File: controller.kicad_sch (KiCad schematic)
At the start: 18 parts, among them SW1 RotaryEncoder_Switch, U6 ATmega328P-P, U7 DS3231MZ

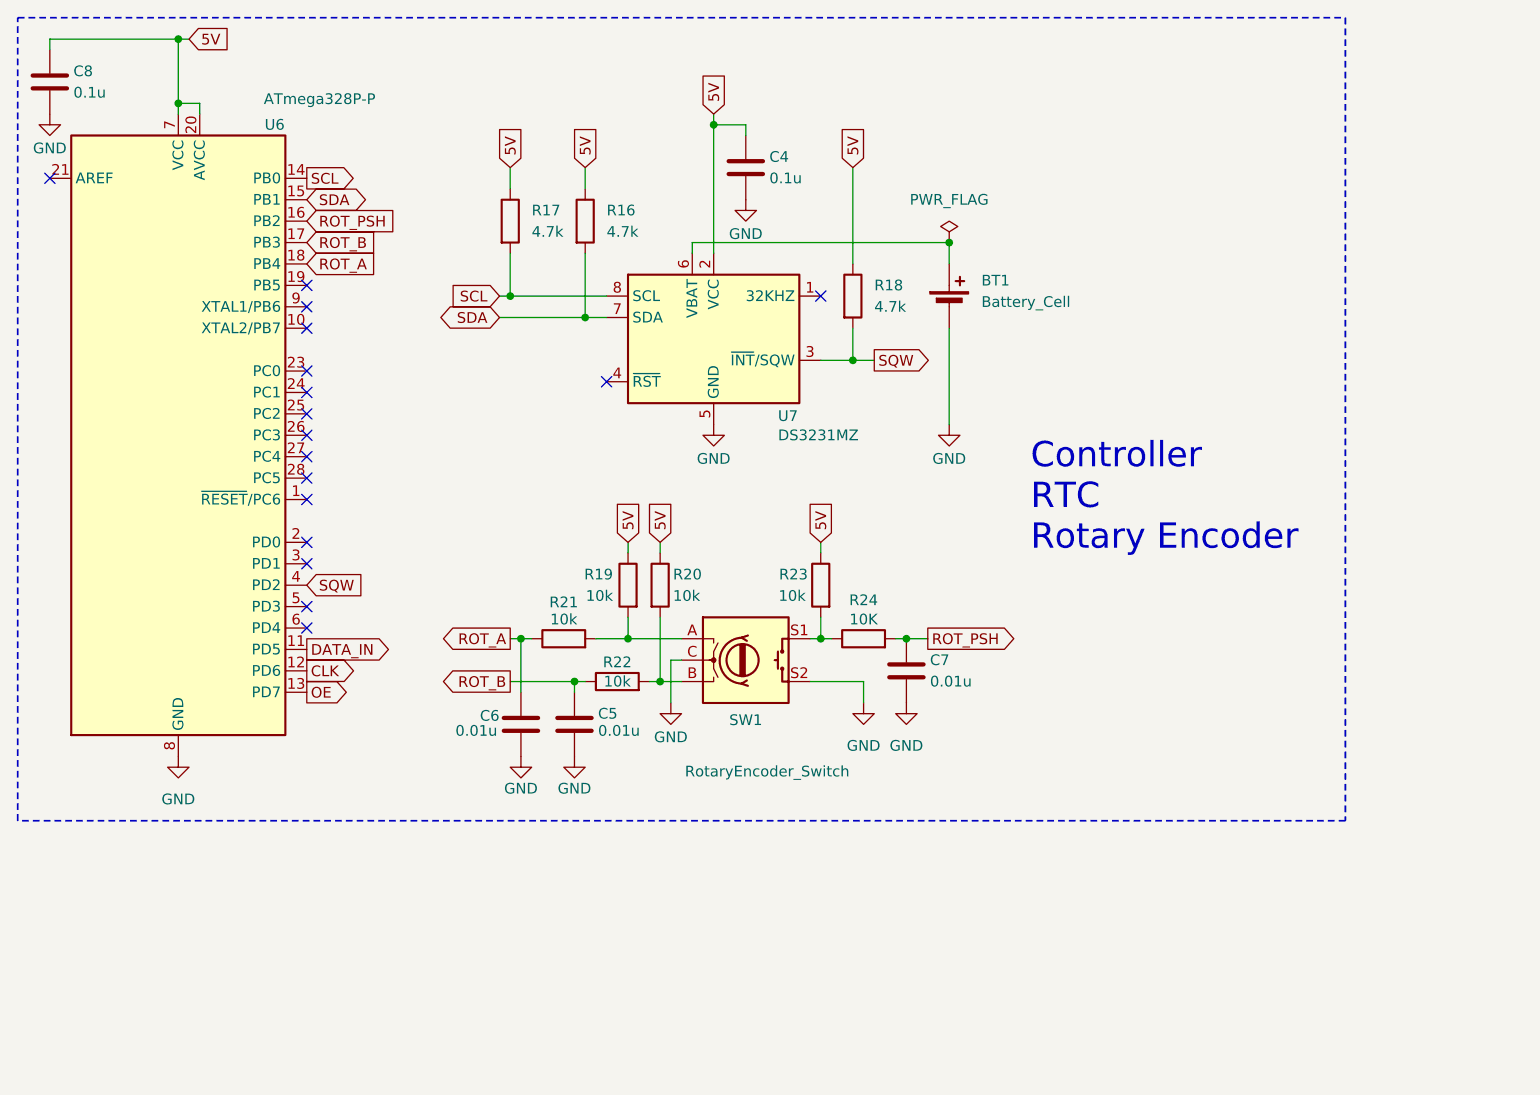
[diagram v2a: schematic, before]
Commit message: added footprints
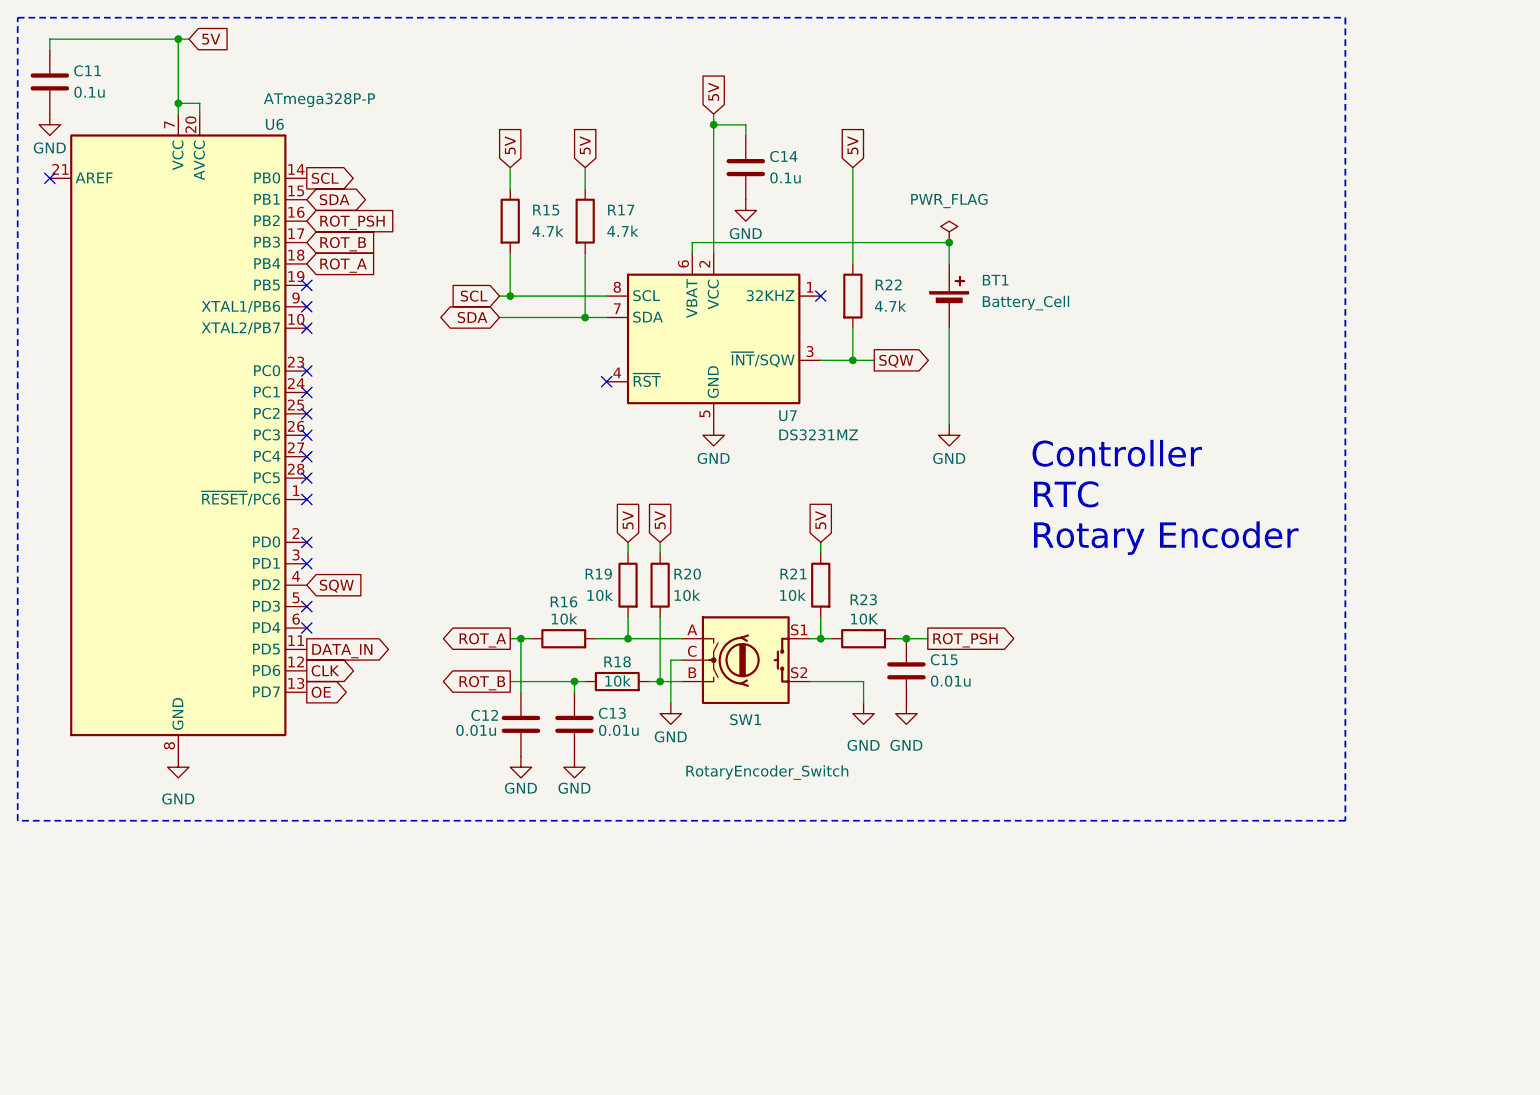
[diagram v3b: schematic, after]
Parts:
- BT1: footprint (none) -> nixie:BH-80B-1
- C11: renamed from C8; footprint (none) -> Capacitor_THT:C_Disc_D4.7mm_W2.5mm_P5.00mm
- C12: renamed from C6; footprint (none) -> Capacitor_THT:C_Disc_D4.7mm_W2.5mm_P5.00mm
- C13: renamed from C5; footprint (none) -> Capacitor_THT:C_Disc_D4.7mm_W2.5mm_P5.00mm
- C14: renamed from C4; footprint (none) -> Capacitor_THT:C_Disc_D4.7mm_W2.5mm_P5.00mm
- C15: renamed from C7; footprint (none) -> Capacitor_THT:C_Disc_D4.7mm_W2.5mm_P5.00mm
- R15: renamed from R17; footprint (none) -> Resistor_THT:R_Axial_DIN0207_L6.3mm_D2.5mm_P7.62mm_Horizontal
- R16: renamed from R21; footprint (none) -> Resistor_THT:R_Axial_DIN0207_L6.3mm_D2.5mm_P7.62mm_Horizontal
- R17: renamed from R16; footprint (none) -> Resistor_THT:R_Axial_DIN0207_L6.3mm_D2.5mm_P7.62mm_Horizontal
- R18: renamed from R22; footprint (none) -> Resistor_THT:R_Axial_DIN0207_L6.3mm_D2.5mm_P7.62mm_Horizontal
- R19, R20: footprint (none) -> Resistor_THT:R_Axial_DIN0207_L6.3mm_D2.5mm_P7.62mm_Horizontal
- R21: renamed from R23; footprint (none) -> Resistor_THT:R_Axial_DIN0207_L6.3mm_D2.5mm_P7.62mm_Horizontal
- R22: renamed from R18; footprint (none) -> Resistor_THT:R_Axial_DIN0207_L6.3mm_D2.5mm_P7.62mm_Horizontal
- R23: renamed from R24; footprint (none) -> Resistor_THT:R_Axial_DIN0207_L6.3mm_D2.5mm_P7.62mm_Horizontal
- SW1: footprint (none) -> nixie:PEC11H4020FS0016
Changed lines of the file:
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@@
 		(dnp no)
 		(fields_autoplaced yes)
-		(property "Reference" "R18"
+		(property "Reference" "R22"
 			(at 115.57 46.9899 0)
 			(effects
@@
 			)
 		)
-		(property "Footprint" ""
+		(property "Footprint" "Resistor_THT:R_Axial_DIN0207_L6.3mm_D2.5mm_P7.62mm_Horizontal"
 			(at 111.252 48.26 90)
 			(effects
@@
 			(project "nixie"
 				(path "/4d215aa3-d175-40c4-bbb4-87e7c6a030b1/e9b2c7e8-8fee-4f00-9fb9-8c32147df66b"
-					(reference "R18")
+					(reference "R22")
 					(unit 1)
 				)
@@
 		(on_board yes)
 		(dnp no)
-		(property "Reference" "#PWR018"
+		(property "Reference" "#PWR022"
 			(at 91.44 102.87 0)
 			(effects
@@
 			(project ""
 				(path "/4d215aa3-d175-40c4-bbb4-87e7c6a030b1/e9b2c7e8-8fee-4f00-9fb9-8c32147df66b"
-					(reference "#PWR018")
+					(reference "#PWR022")
 					(unit 1)
 				)
@@
 		(on_board yes)
 		(dnp no)
-		(property "Reference" "C4"
+		(property "Reference" "C14"
 			(at 103.124 31.75 0)
 			(effects
@@
 			)
 		)
-		(property "Footprint" ""
+		(property "Footprint" "Capacitor_THT:C_Disc_D4.7mm_W2.5mm_P5.00mm"
 			(at 101.2952 36.83 0)
 			(effects
@@
 			(project ""
 				(path "/4d215aa3-d175-40c4-bbb4-87e7c6a030b1/e9b2c7e8-8fee-4f00-9fb9-8c32147df66b"
-					(reference "C4")
+					(reference "C14")
 					(unit 1)
 				)
@@
 		(on_board yes)
 		(dnp no)
-		(property "Reference" "C7"
+		(property "Reference" "C15"
 			(at 122.174 91.44 0)
 			(effects
@@
 			)
 		)
-		(property "Footprint" ""
+		(property "Footprint" "Capacitor_THT:C_Disc_D4.7mm_W2.5mm_P5.00mm"
 			(at 120.3452 96.52 0)
 			(effects
@@
 			(project "nixie"
 				(path "/4d215aa3-d175-40c4-bbb4-87e7c6a030b1/e9b2c7e8-8fee-4f00-9fb9-8c32147df66b"
-					(reference "C7")
+					(reference "C15")
 					(unit 1)
 				)
@@
 			)
 		)
-		(property "Footprint" ""
+		(property "Footprint" "Resistor_THT:R_Axial_DIN0207_L6.3mm_D2.5mm_P7.62mm_Horizontal"
 			(at 88.138 82.55 90)
 			(effects
@@
 		(dnp no)
 		(fields_autoplaced yes)
-		(property "Reference" "#PWR019"
+		(property "Reference" "#PWR025"
 			(at 114.3 102.87 0)
 			(effects
@@
 			(project "nixie"
 				(path "/4d215aa3-d175-40c4-bbb4-87e7c6a030b1/e9b2c7e8-8fee-4f00-9fb9-8c32147df66b"
-					(reference "#PWR019")
+					(reference "#PWR025")
 					(unit 1)
 				)
@@
 		(on_board yes)
 		(dnp no)
-		(property "Reference" "#PWR024"
+		(property "Reference" "#PWR018"
 			(at 17.78 33.02 0)
 			(effects
@@
 			(project "nixie"
 				(path "/4d215aa3-d175-40c4-bbb4-87e7c6a030b1/e9b2c7e8-8fee-4f00-9fb9-8c32147df66b"
-					(reference "#PWR024")
+					(reference "#PWR018")
 					(unit 1)
 				)
@@
 		(on_board yes)
 		(dnp no)
-		(property "Reference" "C8"
+		(property "Reference" "C11"
 			(at 20.574 21.59 0)
 			(effects
@@
 			)
 		)
-		(property "Footprint" ""
+		(property "Footprint" "Capacitor_THT:C_Disc_D4.7mm_W2.5mm_P5.00mm"
 			(at 18.7452 26.67 0)
 			(effects
@@
 			(project "nixie"
 				(path "/4d215aa3-d175-40c4-bbb4-87e7c6a030b1/e9b2c7e8-8fee-4f00-9fb9-8c32147df66b"
-					(reference "C8")
+					(reference "C11")
 					(unit 1)
 				)
@@
 		(dnp no)
 		(fields_autoplaced yes)
-		(property "Reference" "R16"
+		(property "Reference" "R17"
 			(at 83.82 38.0999 0)
 			(effects
@@
 			)
 		)
-		(property "Footprint" ""
+		(property "Footprint" "Resistor_THT:R_Axial_DIN0207_L6.3mm_D2.5mm_P7.62mm_Horizontal"
 			(at 79.502 39.37 90)
 			(effects
@@
 			(project ""
 				(path "/4d215aa3-d175-40c4-bbb4-87e7c6a030b1/e9b2c7e8-8fee-4f00-9fb9-8c32147df66b"
-					(reference "R16")
+					(reference "R17")
 					(unit 1)
 				)
@@
 		(on_board yes)
 		(dnp no)
-		(property "Reference" "R21"
+		(property "Reference" "R16"
 			(at 78.74 84.582 90)
 			(effects
@@
 			)
 		)
-		(property "Footprint" ""
+		(property "Footprint" "Resistor_THT:R_Axial_DIN0207_L6.3mm_D2.5mm_P7.62mm_Horizontal"
 			(at 78.74 90.678 90)
 			(effects
@@
 			(project ""
 				(path "/4d215aa3-d175-40c4-bbb4-87e7c6a030b1/e9b2c7e8-8fee-4f00-9fb9-8c32147df66b"
-					(reference "R21")
+					(reference "R16")
 					(unit 1)
 				)
@@
 		(on_board yes)
 		(dnp no)
-		(property "Reference" "C6"
+		(property "Reference" "C12"
 			(at 71.12 98.044 0)
 			(effects
@@
 			)
 		)
-		(property "Footprint" ""
+		(property "Footprint" "Capacitor_THT:C_Disc_D4.7mm_W2.5mm_P5.00mm"
 			(at 72.6948 102.87 0)
 			(effects
@@
 			(project "nixie"
 				(path "/4d215aa3-d175-40c4-bbb4-87e7c6a030b1/e9b2c7e8-8fee-4f00-9fb9-8c32147df66b"
-					(reference "C6")
+					(reference "C12")
 					(unit 1)
 				)
@@
 		(on_board yes)
 		(dnp no)
-		(property "Reference" "#PWR020"
+		(property "Reference" "#PWR024"
 			(at 100.33 43.18 0)
 			(effects
@@
 			(project ""
 				(path "/4d215aa3-d175-40c4-bbb4-87e7c6a030b1/e9b2c7e8-8fee-4f00-9fb9-8c32147df66b"
-					(reference "#PWR020")
+					(reference "#PWR024")
 					(unit 1)
 				)
@@
 		(on_board yes)
 		(dnp no)
-		(property "Reference" "#PWR016"
+		(property "Reference" "#PWR023"
 			(at 96.52 69.85 0)
 			(effects
@@
 			(project "nixie"
 				(path "/4d215aa3-d175-40c4-bbb4-87e7c6a030b1/e9b2c7e8-8fee-4f00-9fb9-8c32147df66b"
-					(reference "#PWR016")
+					(reference "#PWR023")
 					(unit 1)
 				)
@@
 		(dnp no)
 		(fields_autoplaced yes)
-		(property "Reference" "#PWR023"
+		(property "Reference" "#PWR026"
 			(at 119.38 102.87 0)
 			(effects
@@
 			(project "nixie"
 				(path "/4d215aa3-d175-40c4-bbb4-87e7c6a030b1/e9b2c7e8-8fee-4f00-9fb9-8c32147df66b"
-					(reference "#PWR023")
+					(reference "#PWR026")
 					(unit 1)
 				)
@@
 		(on_board yes)
 		(dnp no)
-		(property "Reference" "C5"
+		(property "Reference" "C13"
 			(at 82.804 97.79 0)
 			(effects
@@
 			)
 		)
-		(property "Footprint" ""
+		(property "Footprint" "Capacitor_THT:C_Disc_D4.7mm_W2.5mm_P5.00mm"
 			(at 80.9752 102.87 0)
 			(effects
@@
 			(project ""
 				(path "/4d215aa3-d175-40c4-bbb4-87e7c6a030b1/e9b2c7e8-8fee-4f00-9fb9-8c32147df66b"
-					(reference "C5")
+					(reference "C13")
 					(unit 1)
 				)
@@
 		(dnp no)
 		(fields_autoplaced yes)
-		(property "Reference" "#PWR01"
+		(property "Reference" "#PWR019"
 			(at 33.02 109.22 0)
 			(effects
@@
 			(project ""
 				(path "/4d215aa3-d175-40c4-bbb4-87e7c6a030b1/e9b2c7e8-8fee-4f00-9fb9-8c32147df66b"
-					(reference "#PWR01")
+					(reference "#PWR019")
 					(unit 1)
 				)
@@
 			)
 		)
-		(property "Footprint" ""
+		(property "Footprint" "nixie:PEC11H4020FS0016"
 			(at 96.52 87.376 0)
 			(effects
@@
 		(on_board yes)
 		(dnp no)
-		(property "Reference" "R24"
+		(property "Reference" "R23"
 			(at 114.3 84.328 90)
 			(effects
@@
 			)
 		)
-		(property "Footprint" ""
+		(property "Footprint" "Resistor_THT:R_Axial_DIN0207_L6.3mm_D2.5mm_P7.62mm_Horizontal"
 			(at 114.3 90.678 90)
 			(effects
@@
 			(project ""
 				(path "/4d215aa3-d175-40c4-bbb4-87e7c6a030b1/e9b2c7e8-8fee-4f00-9fb9-8c32147df66b"
-					(reference "R24")
+					(reference "R23")
 					(unit 1)
 				)
@@
 		(on_board yes)
 		(dnp no)
-		(property "Reference" "R23"
+		(property "Reference" "R21"
 			(at 107.696 81.28 0)
 			(effects
@@
 			)
 		)
-		(property "Footprint" ""
+		(property "Footprint" "Resistor_THT:R_Axial_DIN0207_L6.3mm_D2.5mm_P7.62mm_Horizontal"
 			(at 110.998 82.55 90)
 			(effects
@@
 			(project "nixie"
 				(path "/4d215aa3-d175-40c4-bbb4-87e7c6a030b1/e9b2c7e8-8fee-4f00-9fb9-8c32147df66b"
-					(reference "R23")
+					(reference "R21")
 					(unit 1)
 				)
@@
 		(dnp no)
 		(fields_autoplaced yes)
-		(property "Reference" "R17"
+		(property "Reference" "R15"
 			(at 74.93 38.0999 0)
 			(effects
@@
 			)
 		)
-		(property "Footprint" ""
+		(property "Footprint" "Resistor_THT:R_Axial_DIN0207_L6.3mm_D2.5mm_P7.62mm_Horizontal"
 			(at 70.612 39.37 90)
 			(effects
@@
 			(project "nixie"
 				(path "/4d215aa3-d175-40c4-bbb4-87e7c6a030b1/e9b2c7e8-8fee-4f00-9fb9-8c32147df66b"
-					(reference "R17")
+					(reference "R15")
 					(unit 1)
 				)
@@
 			)
 		)
-		(property "Footprint" ""
+		(property "Footprint" "Resistor_THT:R_Axial_DIN0207_L6.3mm_D2.5mm_P7.62mm_Horizontal"
 			(at 88.392 82.55 90)
 			(effects
@@
 		(on_board yes)
 		(dnp no)
-		(property "Reference" "#PWR021"
+		(property "Reference" "#PWR020"
 			(at 73.66 109.22 0)
 			(effects
@@
 			(project "nixie"
 				(path "/4d215aa3-d175-40c4-bbb4-87e7c6a030b1/e9b2c7e8-8fee-4f00-9fb9-8c32147df66b"
-					(reference "#PWR021")
+					(reference "#PWR020")
 					(unit 1)
 				)
@@
 		(on_board yes)
 		(dnp no)
-		(property "Reference" "#PWR017"
+		(property "Reference" "#PWR027"
 			(at 124.46 69.85 0)
 			(effects
@@
 			(project "nixie"
 				(path "/4d215aa3-d175-40c4-bbb4-87e7c6a030b1/e9b2c7e8-8fee-4f00-9fb9-8c32147df66b"
-					(reference "#PWR017")
+					(reference "#PWR027")
 					(unit 1)
 				)
@@
 			)
 		)
-		(property "Footprint" ""
+		(property "Footprint" "nixie:BH-80B-1"
 			(at 124.46 48.006 90)
 			(effects
@@
 		(on_board yes)
 		(dnp no)
-		(property "Reference" "#PWR022"
+		(property "Reference" "#PWR021"
 			(at 80.01 109.22 0)
 			(effects
@@
 			(project "nixie"
 				(path "/4d215aa3-d175-40c4-bbb4-87e7c6a030b1/e9b2c7e8-8fee-4f00-9fb9-8c32147df66b"
-					(reference "#PWR022")
+					(reference "#PWR021")
 					(unit 1)
 				)
@@
 		(on_board yes)
 		(dnp no)
-		(property "Reference" "R22"
+		(property "Reference" "R18"
 			(at 85.09 91.694 90)
 			(effects
@@
 			)
 		)
-		(property "Footprint" ""
+		(property "Footprint" "Resistor_THT:R_Axial_DIN0207_L6.3mm_D2.5mm_P7.62mm_Horizontal"
 			(at 85.09 95.758 90)
 			(effects
@@
 			(project "nixie"
 				(path "/4d215aa3-d175-40c4-bbb4-87e7c6a030b1/e9b2c7e8-8fee-4f00-9fb9-8c32147df66b"
-					(reference "R22")
-					(unit 1)
-				)
+					(reference "R18")
+					(unit 1)
+				)

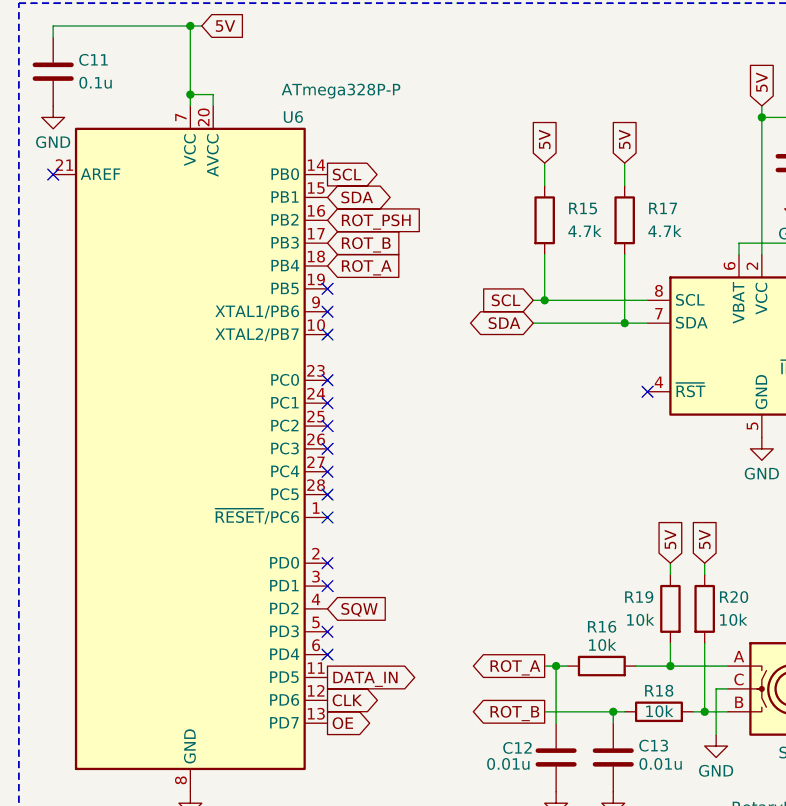
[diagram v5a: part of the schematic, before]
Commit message: connect scl sda to correct pins
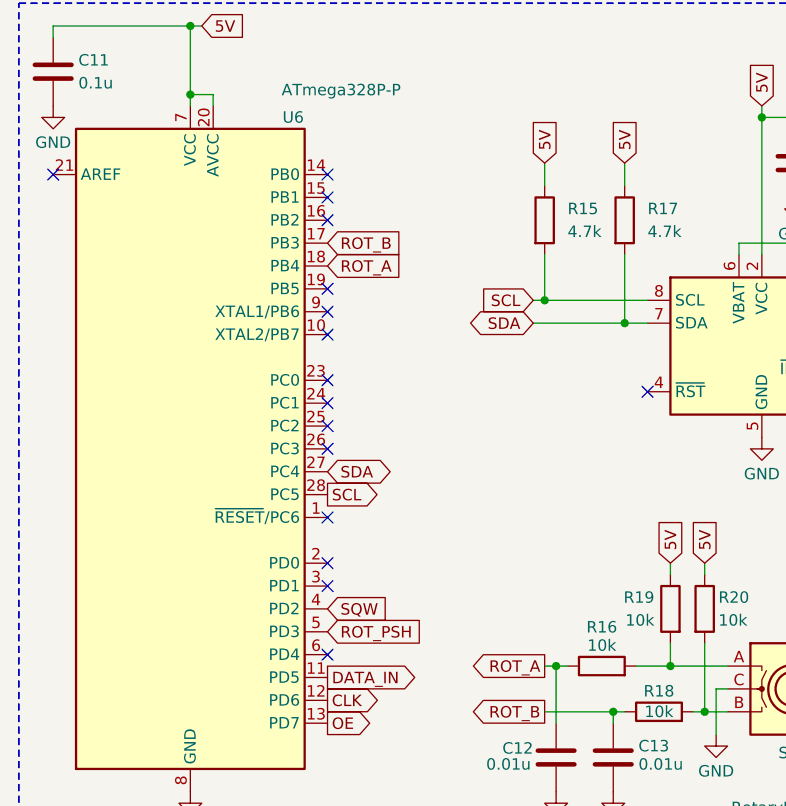
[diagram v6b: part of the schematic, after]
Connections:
- net ROT_PSH: now also U6.5 (PD3); no longer U6.16 (PB2)
- net SCL: now also U6.28 (PC5); no longer U6.14 (PB0)
- net SDA: now also U6.27 (PC4); no longer U6.15 (PB1)
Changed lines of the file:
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@@
+	)
+	(no_connect
+		(at 48.26 34.29)
 	)
 	(no_connect
@@
 	)
 	(no_connect
-		(at 48.26 85.09)
-	)
-	(no_connect
 		(at 48.26 77.47)
 	)
@@
 	)
 	(no_connect
+		(at 48.26 36.83)
+	)
+	(no_connect
 		(at 48.26 52.07)
 	)
 	(no_connect
-		(at 48.26 67.31)
-	)
-	(no_connect
 		(at 48.26 59.69)
 	)
@@
 	)
 	(no_connect
+		(at 48.26 39.37)
+	)
+	(no_connect
 		(at 17.78 34.29)
-	)
-	(no_connect
-		(at 48.26 69.85)
 	)
 	(wire
@@
 	(global_label "SDA"
 		(shape bidirectional)
-		(at 48.26 36.83 0)
-		(fields_autoplaced yes)
-		(effects
-			(font
-				(size 1.27 1.27)
-			)
-			(justify left)
-		)
-		(property "Intersheetrefs" "${INTERSHEET_REFS}"
-			(at 55.9246 36.83 0)
+		(at 48.26 67.31 0)
+		(fields_autoplaced yes)
+		(effects
+			(font
+				(size 1.27 1.27)
+			)
+			(justify left)
+		)
+		(property "Intersheetrefs" "${INTERSHEET_REFS}"
+			(at 55.9246 67.31 0)
 			(effects
 				(font
@@
 	(global_label "SCL"
 		(shape output)
-		(at 48.26 34.29 0)
-		(fields_autoplaced yes)
-		(effects
-			(font
-				(size 1.27 1.27)
-			)
-			(justify left)
-		)
-		(property "Intersheetrefs" "${INTERSHEET_REFS}"
-			(at 54.7528 34.29 0)
+		(at 48.26 69.85 0)
+		(fields_autoplaced yes)
+		(effects
+			(font
+				(size 1.27 1.27)
+			)
+			(justify left)
+		)
+		(property "Intersheetrefs" "${INTERSHEET_REFS}"
+			(at 54.7528 69.85 0)
 			(effects
 				(font
@@
 	(global_label "ROT_PSH"
 		(shape input)
-		(at 48.26 39.37 0)
-		(fields_autoplaced yes)
-		(effects
-			(font
-				(size 1.27 1.27)
-			)
-			(justify left)
-		)
-		(property "Intersheetrefs" "${INTERSHEET_REFS}"
-			(at 59.5909 39.37 0)
-			(effects
-				(font
+		(at 48.26 85.09 0)
+		(fields_autoplaced yes)
+		(effects
+			(font
+				(size 1.27 1.27)
+			)
+			(justify left)
+		)
+		(property "Intersheetrefs" "${INTERSHEET_REFS}"
+			(at 59.5909 85.09 0)
+			(effects
+				(font
